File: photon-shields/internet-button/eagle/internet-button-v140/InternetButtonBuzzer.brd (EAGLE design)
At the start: 65.5 x 65.5 mm, 41 parts

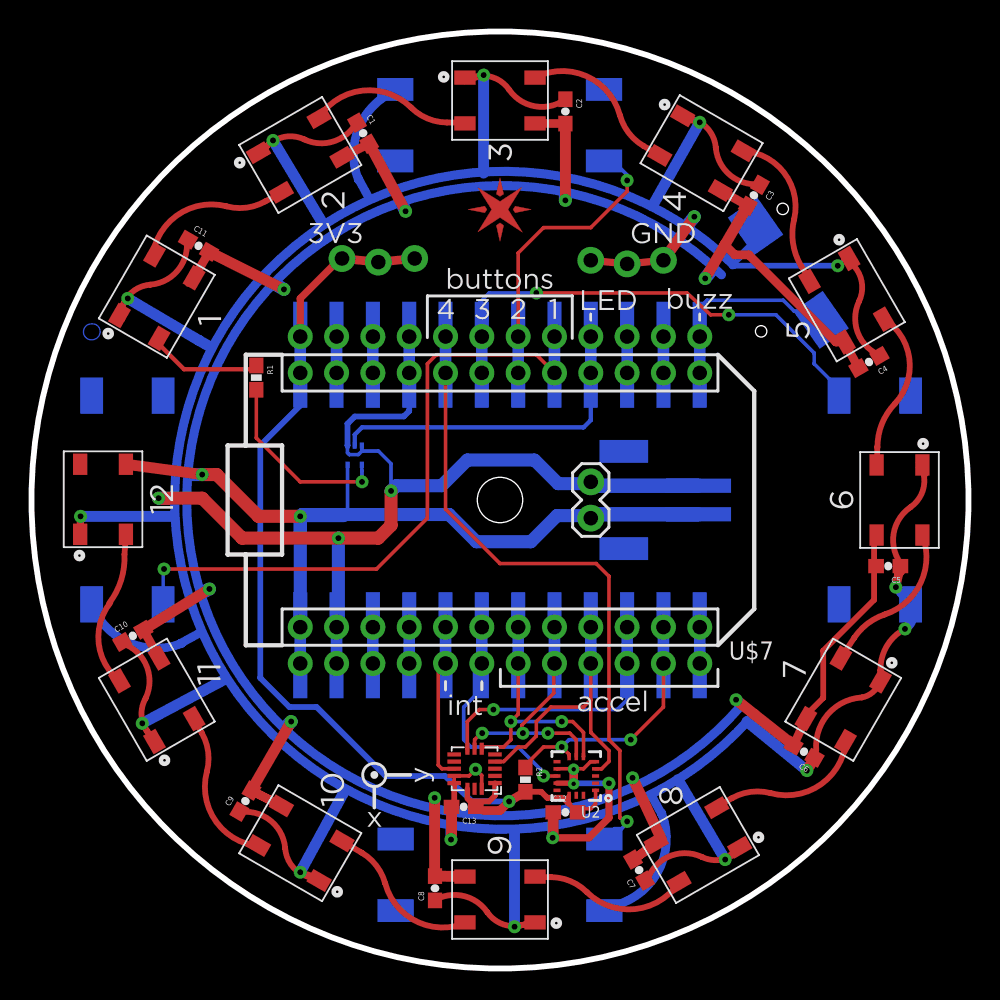
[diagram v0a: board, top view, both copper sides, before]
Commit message: update the arrow for silkscreen
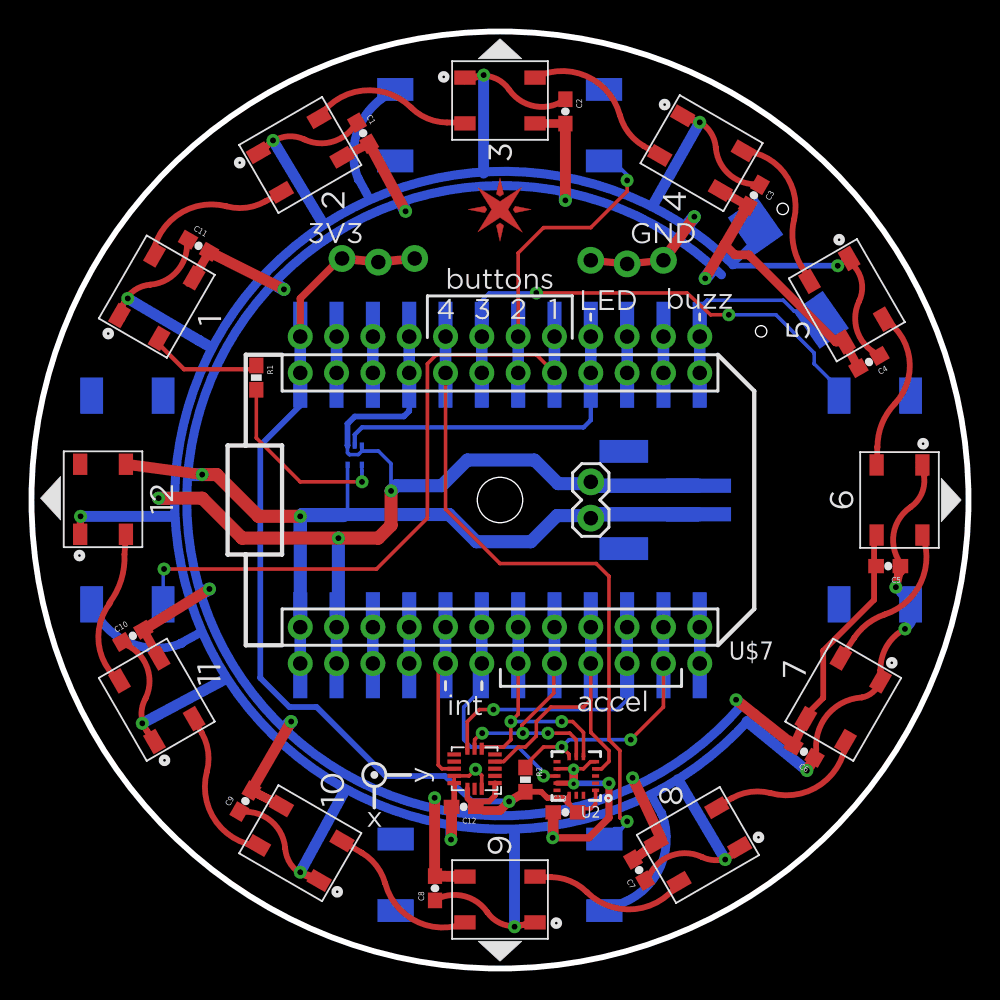
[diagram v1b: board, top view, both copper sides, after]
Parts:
- moved C12 7.12 mm to (31.8, 11.6), turned to 180 degrees
- moved C13 7.12 mm to (38.9, 11.2), turned to 0 degrees
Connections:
- net +3V3: now also C12.1, C13.2; no longer C12.2, C13.1
- net GND: now also C12.2, C13.1; no longer C12.1, C13.2
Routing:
- removed copper zone on layer 16, net N$3
